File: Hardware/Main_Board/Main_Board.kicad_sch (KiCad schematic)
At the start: 0 parts

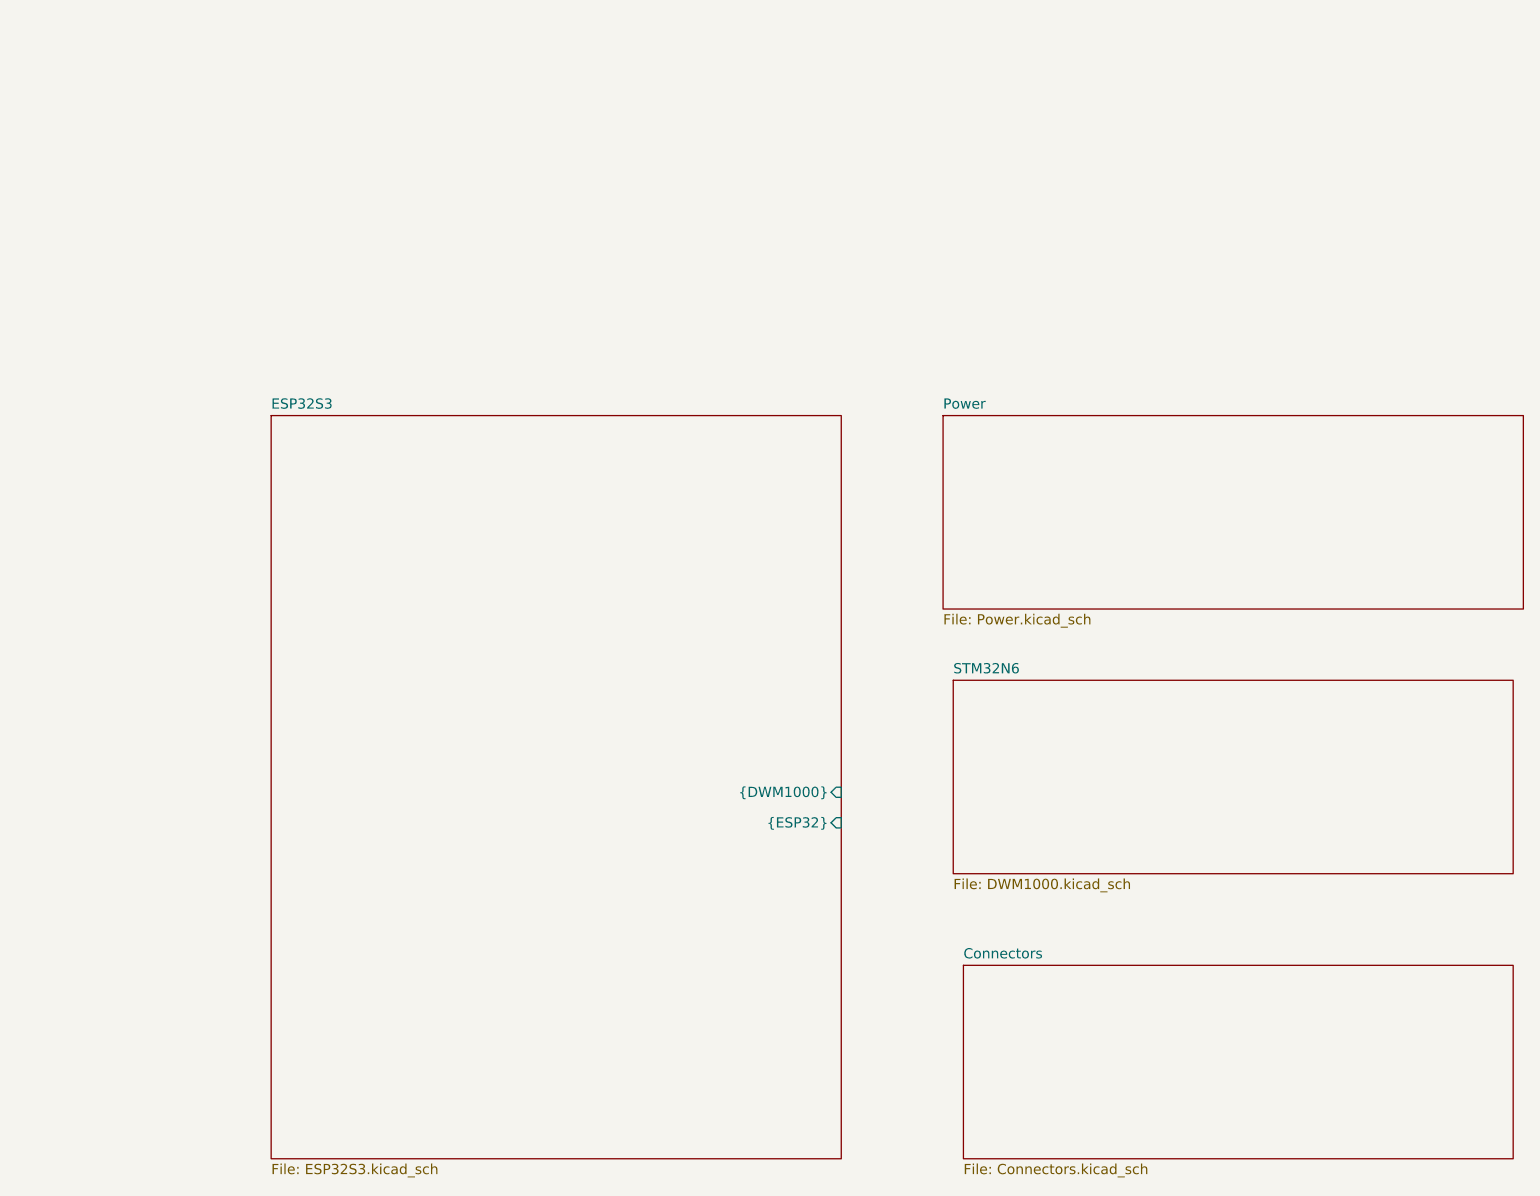
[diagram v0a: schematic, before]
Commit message: finished most of the main board
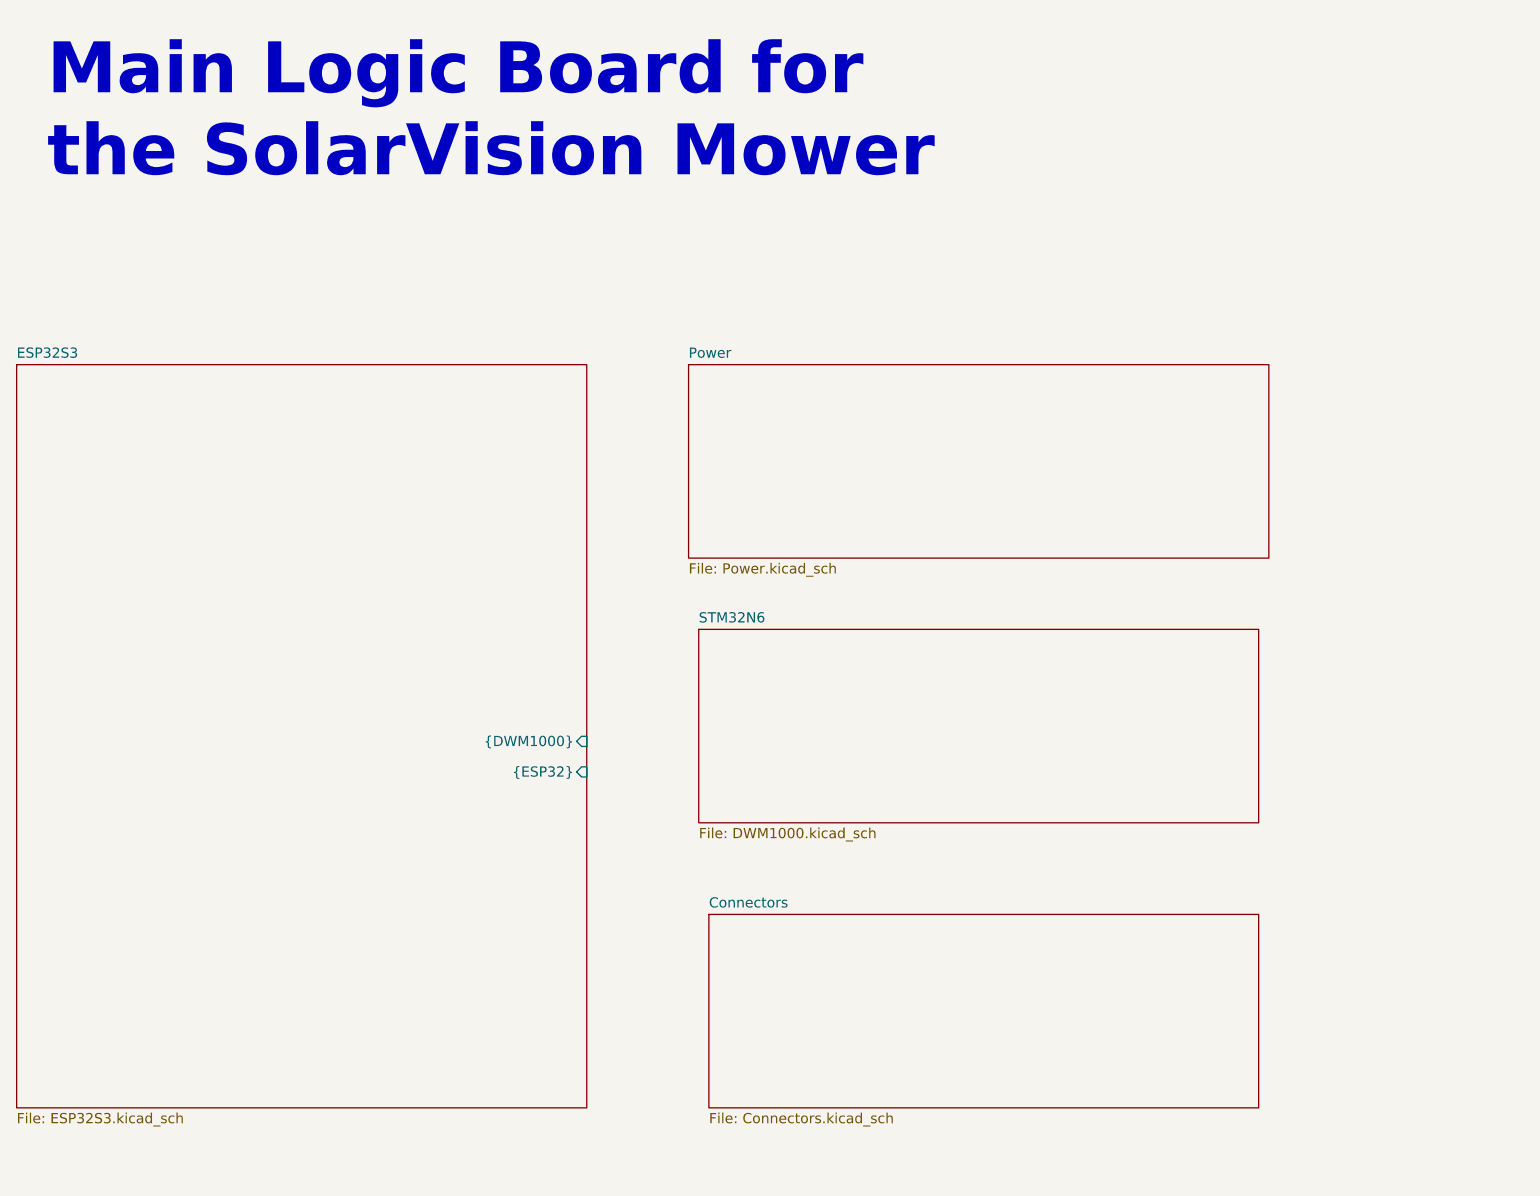
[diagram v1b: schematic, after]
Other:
- note added: "Main Logic Board for the SolarVision Mower"
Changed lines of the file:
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@@
 		(members "GPIO[0..48]" "RST")
 	)
+	(text "Main Logic Board for\nthe SolarVision Mower"
+		(exclude_from_sim no)
+		(at 20.32 23.114 0)
+		(effects
+			(font
+				(size 6.35 6.35)
+				(thickness 1.27)
+				(bold yes)
+			)
+			(justify left top)
+		)
+	)
 	(sheet
-		(at 134.62 138.43)
+		(at 102.87 132.08)
 		(size 68.58 24.13)
 		(exclude_from_sim no)
@@
 		)
 		(property "Sheetname" "Connectors"
-			(at 134.62 137.7184 0)
+			(at 102.87 131.3684 0)
 			(effects
 				(font
@@
 		)
 		(property "Sheetfile" "Connectors.kicad_sch"
-			(at 134.62 163.1446 0)
+			(at 102.87 156.7946 0)
 			(effects
 				(font
@@
 	)
 	(sheet
-		(at 133.35 102.87)
+		(at 101.6 96.52)
 		(size 69.85 24.13)
 		(exclude_from_sim no)
@@
 		)
 		(property "Sheetname" "STM32N6"
-			(at 133.35 102.1584 0)
+			(at 101.6 95.8084 0)
 			(effects
 				(font
@@
 		)
 		(property "Sheetfile" "DWM1000.kicad_sch"
-			(at 133.35 127.5846 0)
+			(at 101.6 121.2346 0)
 			(effects
 				(font
@@
 	)
 	(sheet
-		(at 132.08 69.85)
+		(at 100.33 63.5)
 		(size 72.39 24.13)
 		(exclude_from_sim no)
@@
 		)
 		(property "Sheetname" "Power"
-			(at 132.08 69.1384 0)
+			(at 100.33 62.7884 0)
 			(effects
 				(font
@@
 		)
 		(property "Sheetfile" "Power.kicad_sch"
-			(at 132.08 94.5646 0)
+			(at 100.33 88.2146 0)
 			(effects
 				(font
@@
 	)
 	(sheet
-		(at 48.26 69.85)
+		(at 16.51 63.5)
 		(size 71.12 92.71)
 		(exclude_from_sim no)
@@
 		)
 		(property "Sheetname" "ESP32S3"
-			(at 48.26 69.1384 0)
+			(at 16.51 62.7884 0)
 			(effects
 				(font
@@
 		)
 		(property "Sheetfile" "ESP32S3.kicad_sch"
-			(at 48.26 163.1446 0)
+			(at 16.51 156.7946 0)
 			(effects
 				(font
@@
 		)
 		(pin "{DWM1000}" input
-			(at 119.38 116.84 0)
+			(at 87.63 110.49 0)
 			(effects
 				(font
@@
 		)
 		(pin "{ESP32}" input
-			(at 119.38 120.65 0)
+			(at 87.63 114.3 0)
 			(effects
 				(font

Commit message: added gerbers, drill files, BOM and CPL for the main board
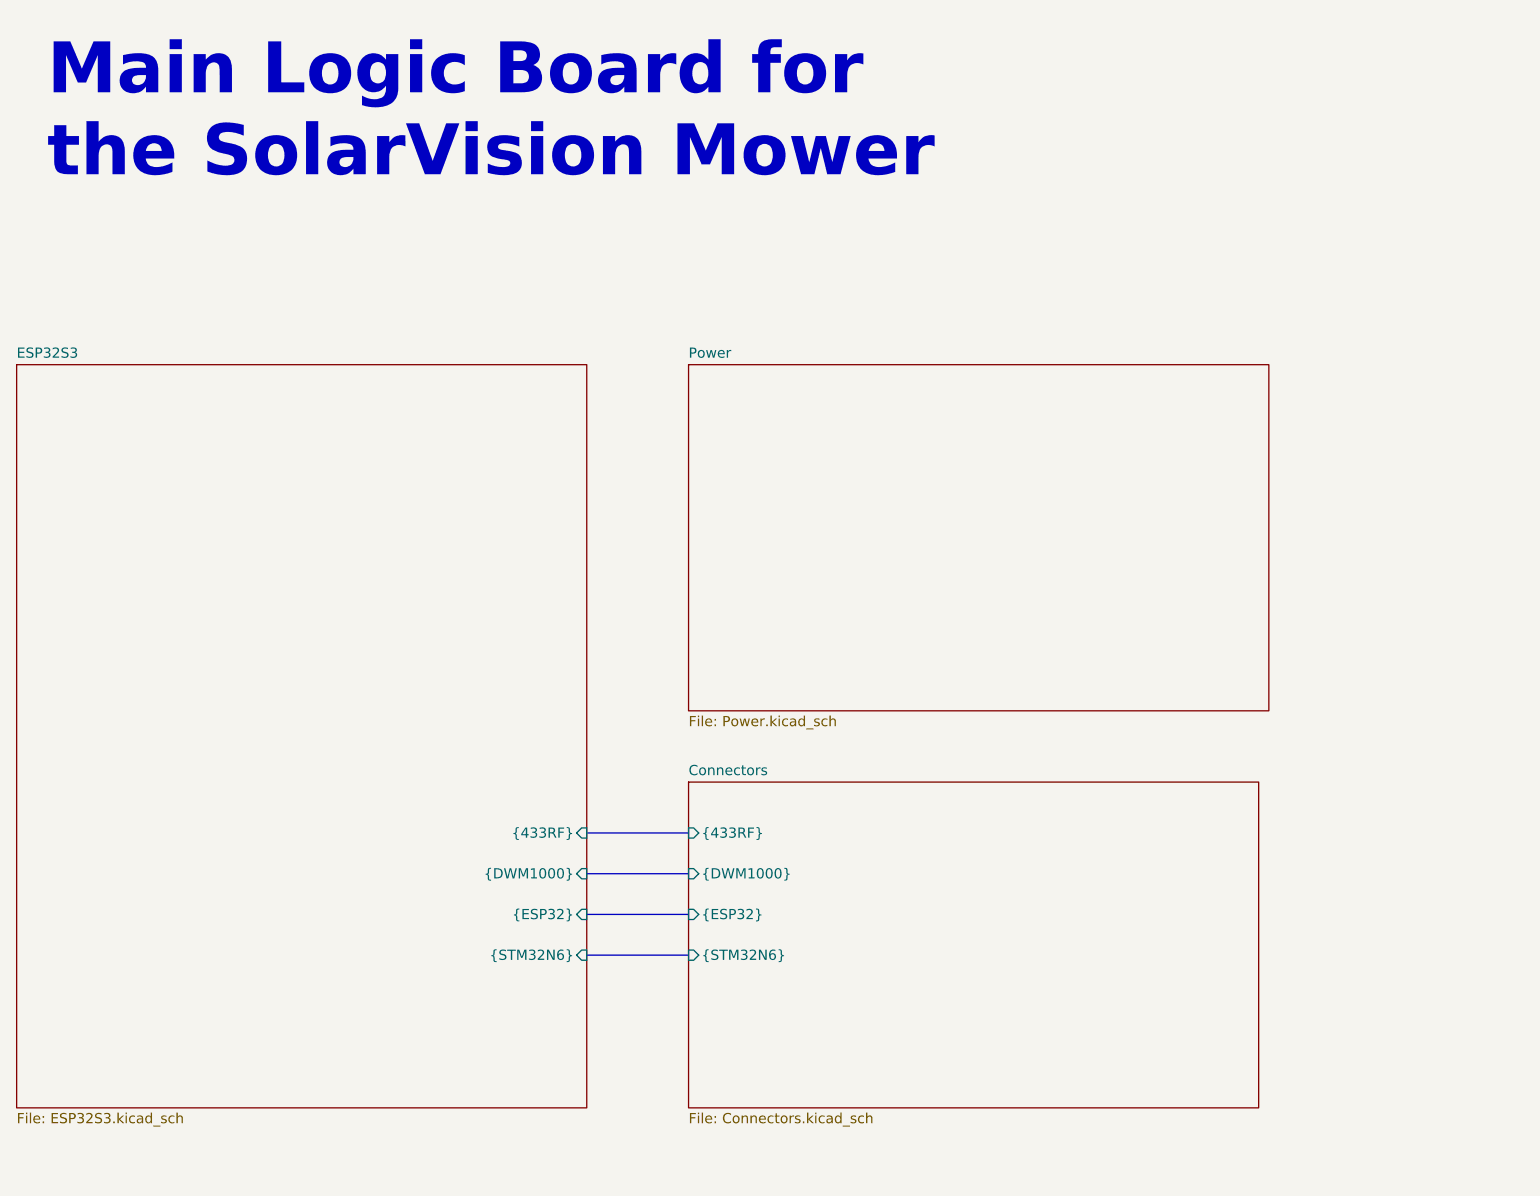
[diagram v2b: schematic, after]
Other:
- removed sheet STM32N6
- sheet Connectors ports: added {433RF}, {DWM1000}, {ESP32}, {STM32N6}; removed none
- sheet ESP32S3 ports: added {433RF}, {STM32N6}; removed none
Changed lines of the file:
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@@
 	(generator_version "9.0")
 	(paper "A4")
+	(bus_alias "433RF"
+		(members "RF_RX" "RF_TX" "SET")
+	)
 	(bus_alias "ESP32"
 		(members "GPIO[0..48]" "RST")
@@
 		)
 	)
+	(bus
+		(pts
+			(xy 87.63 137.16) (xy 100.33 137.16)
+		)
+		(stroke
+			(width 0)
+			(type default)
+		)
+	)
+	(bus
+		(pts
+			(xy 87.63 132.08) (xy 100.33 132.08)
+		)
+		(stroke
+			(width 0)
+			(type default)
+		)
+	)
+	(bus
+		(pts
+			(xy 87.63 121.92) (xy 100.33 121.92)
+		)
+		(stroke
+			(width 0)
+			(type default)
+		)
+	)
+	(bus
+		(pts
+			(xy 87.63 127) (xy 100.33 127)
+		)
+		(stroke
+			(width 0)
+			(type default)
+		)
+	)
 	(sheet
-		(at 102.87 132.08)
-		(size 68.58 24.13)
+		(at 100.33 115.57)
+		(size 71.12 40.64)
 		(exclude_from_sim no)
 		(in_bom yes)
@@
 		)
 		(property "Sheetname" "Connectors"
-			(at 102.87 131.3684 0)
+			(at 100.33 114.8584 0)
 			(effects
 				(font
@@
 		)
 		(property "Sheetfile" "Connectors.kicad_sch"
-			(at 102.87 156.7946 0)
+			(at 100.33 156.7946 0)
 			(effects
 				(font
@@
 				)
 				(justify left top)
+			)
+		)
+		(pin "{433RF}" input
+			(at 100.33 121.92 180)
+			(effects
+				(font
+					(size 1.27 1.27)
+				)
+				(justify left)
+			)
+		)
+		(pin "{DWM1000}" input
+			(at 100.33 127 180)
+			(effects
+				(font
+					(size 1.27 1.27)
+				)
+				(justify left)
+			)
+		)
+		(pin "{ESP32}" input
+			(at 100.33 132.08 180)
+			(effects
+				(font
+					(size 1.27 1.27)
+				)
+				(justify left)
+			)
+		)
+		(pin "{STM32N6}" input
+			(at 100.33 137.16 180)
+			(effects
+				(font
+					(size 1.27 1.27)
+				)
+				(justify left)
 			)
 		)
@@
 	)
 	(sheet
-		(at 101.6 96.52)
-		(size 69.85 24.13)
+		(at 100.33 63.5)
+		(size 72.39 43.18)
 		(exclude_from_sim no)
 		(in_bom yes)
@@
 			(color 0 221 221 1.0000)
 		)
-		(property "Sheetname" "STM32N6"
-			(at 101.6 95.8084 0)
+		(property "Sheetname" "Power"
+			(at 100.33 62.7884 0)
 			(effects
 				(font
@@
 			)
 		)
-		(property "Sheetfile" "DWM1000.kicad_sch"
-			(at 101.6 121.2346 0)
+		(property "Sheetfile" "Power.kicad_sch"
+			(at 100.33 107.2646 0)
 			(effects
 				(font
@@
 			(project "Main_Board"
 				(path "/3bfaeaa6-4337-4b5f-9f42-0e28df6ecb69"
-					(page "3")
+					(page "4")
 				)
 			)
@@
 	)
 	(sheet
-		(at 100.33 63.5)
-		(size 72.39 24.13)
+		(at 16.51 63.5)
+		(size 71.12 92.71)
 		(exclude_from_sim no)
 		(in_bom yes)
@@
 			(color 0 221 221 1.0000)
 		)
-		(property "Sheetname" "Power"
-			(at 100.33 62.7884 0)
-			(effects
-				(font
-					(size 1.27 1.27)
-				)
-				(justify left bottom)
-			)
-		)
-		(property "Sheetfile" "Power.kicad_sch"
-			(at 100.33 88.2146 0)
-			(effects
-				(font
-					(size 1.27 1.27)
-				)
-				(justify left top)
-			)
-		)
-		(instances
-			(project "Main_Board"
-				(path "/3bfaeaa6-4337-4b5f-9f42-0e28df6ecb69"
-					(page "4")
-				)
-			)
-		)
-	)
-	(sheet
-		(at 16.51 63.5)
-		(size 71.12 92.71)
-		(exclude_from_sim no)
-		(in_bom yes)
-		(on_board yes)
-		(dnp no)
-		(fields_autoplaced yes)
-		(stroke
-			(width 0.1524)
-			(type solid)
-		)
-		(fill
-			(color 0 221 221 1.0000)
-		)
 		(property "Sheetname" "ESP32S3"
 			(at 16.51 62.7884 0)
@@
 		)
 		(pin "{DWM1000}" input
-			(at 87.63 110.49 0)
+			(at 87.63 127 0)
 			(effects
 				(font
@@
 		)
 		(pin "{ESP32}" input
-			(at 87.63 114.3 0)
-			(effects
-				(font
+			(at 87.63 132.08 0)
+			(effects
+				(font
+					(size 1.27 1.27)
+				)
+				(justify right)
+			)
+		)
+		(pin "{433RF}" input
+			(at 87.63 121.92 0)
+			(effects
+				(font
+					(size 1.27 1.27)
+				)
+				(justify right)
+			)
+		)
+		(pin "{STM32N6}" input
+			(at 87.63 137.16 0)
+			(effects
+				(font
